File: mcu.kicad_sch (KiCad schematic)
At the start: 22 parts, among them J1 SWD_DBG, U1 STM32F405RGTx, Y1 8MHz, Y2 32.768kHz

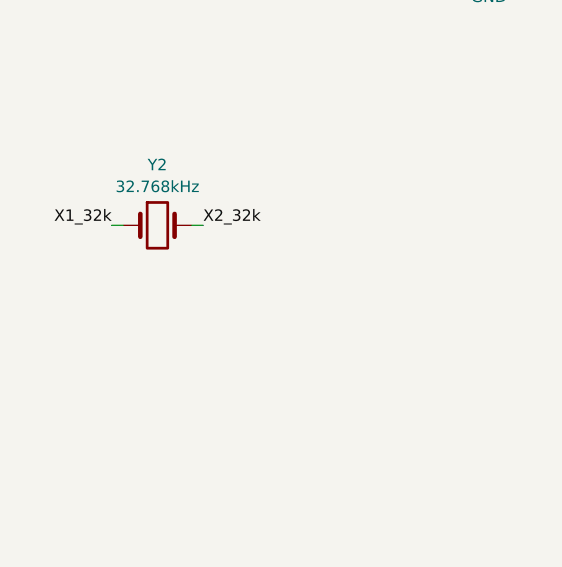
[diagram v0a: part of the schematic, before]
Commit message: fixes
- USB-C closer to the board's edge
- added 20pF caps for the 32.768kHz resonator
- replaced ferrite beads with 0805-sized ones
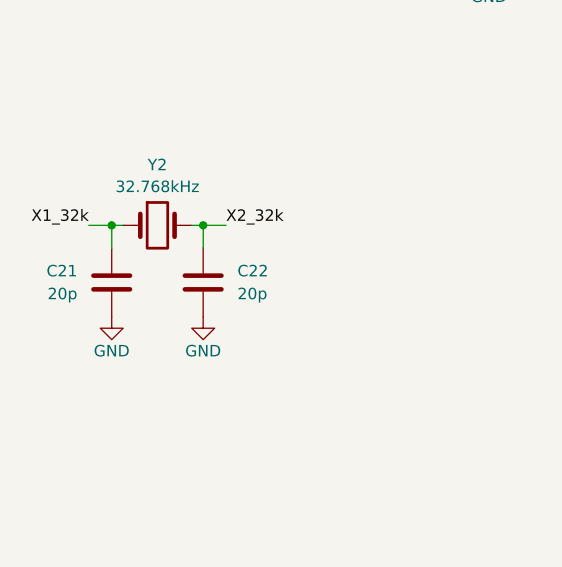
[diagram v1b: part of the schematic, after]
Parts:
- added C21, C22: 20p, Capacitor_SMD:C_0402_1005Metric, symbol Device:C
- FB1, FB2: MPN 81-NFZ2MSD102SZ10L -> 810-MPZ2012S102AT000; PN 81-NFZ2MSD102SZ10L -> 810-MPZ2012S102AT000
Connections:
- net GND: now also C21.2, C22.1
- net X1_32k: now also C21.1
- net X2_32k: now also C22.2
